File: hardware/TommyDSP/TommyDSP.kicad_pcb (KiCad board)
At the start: 2 copper layers, 85 x 85 mm, 143 parts, among them J401 Conn_01x02_Pin, J501 USB_C_Receptacle_USB2.0_16P, J502 AudioJack3_SwitchTR, J503 XH-2.50mm Horizontal, J504 AudioJack3_SwitchTR, J505 EXT.IN, J506 AudioJack3_SwitchTR, J507 XH-2.50mm Horizontal, J508 EXT.OUT, J509 Conn_01x03_Pin, J510 AudioJack3_SwitchTR, J511 Micro_SD_Card_Det1, J512 Qwiic, Q401 AO3401A, SW201 SW_Push, SW202 SW_Push, SW501 RotaryEncoder_Switch_MP, U201 W25Q128JVS, U202 DNF, U203 RP2350_60QFN, U301 ES8388, U401 TPS7A2033PDBVR, U402 TPS62A01APDDC, U403 TP4056-42-ESOP8, Y201 ABM8-272-T3

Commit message: hardware: minor tweaks
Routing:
- net GND: vias 815 -> 820

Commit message: hardware: minor tweaks
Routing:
- net GND: vias 820 -> 824
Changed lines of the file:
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@@
 	)
 	(via
+		(at 147.575 82.1)
+		(size 0.6)
+		(drill 0.3)
+		(layers "F.Cu" "B.Cu")
+		(free yes)
+		(net 2)
+	)
+	(via
 		(at 123 136.55)
 		(size 0.6)
@@
 	)
 	(via
+		(at 142.65 81.55)
+		(size 0.6)
+		(drill 0.3)
+		(layers "F.Cu" "B.Cu")
+		(free yes)
+		(net 2)
+	)
+	(via
 		(at 162.695 141.01)
 		(size 0.6)
@@
 	)
 	(via
+		(at 122.7 87.05)
+		(size 0.6)
+		(drill 0.3)
+		(layers "F.Cu" "B.Cu")
+		(free yes)
+		(net 2)
+	)
+	(via
 		(at 195.715 143.55)
 		(size 0.6)
@@
 		(size 0.6)
 		(drill 0.3)
+		(layers "F.Cu" "B.Cu")
+		(free yes)
+		(net 2)
+	)
+	(via
+		(at 138.25 81.575)
+		(size 0.6)
+		(drill 0.3)

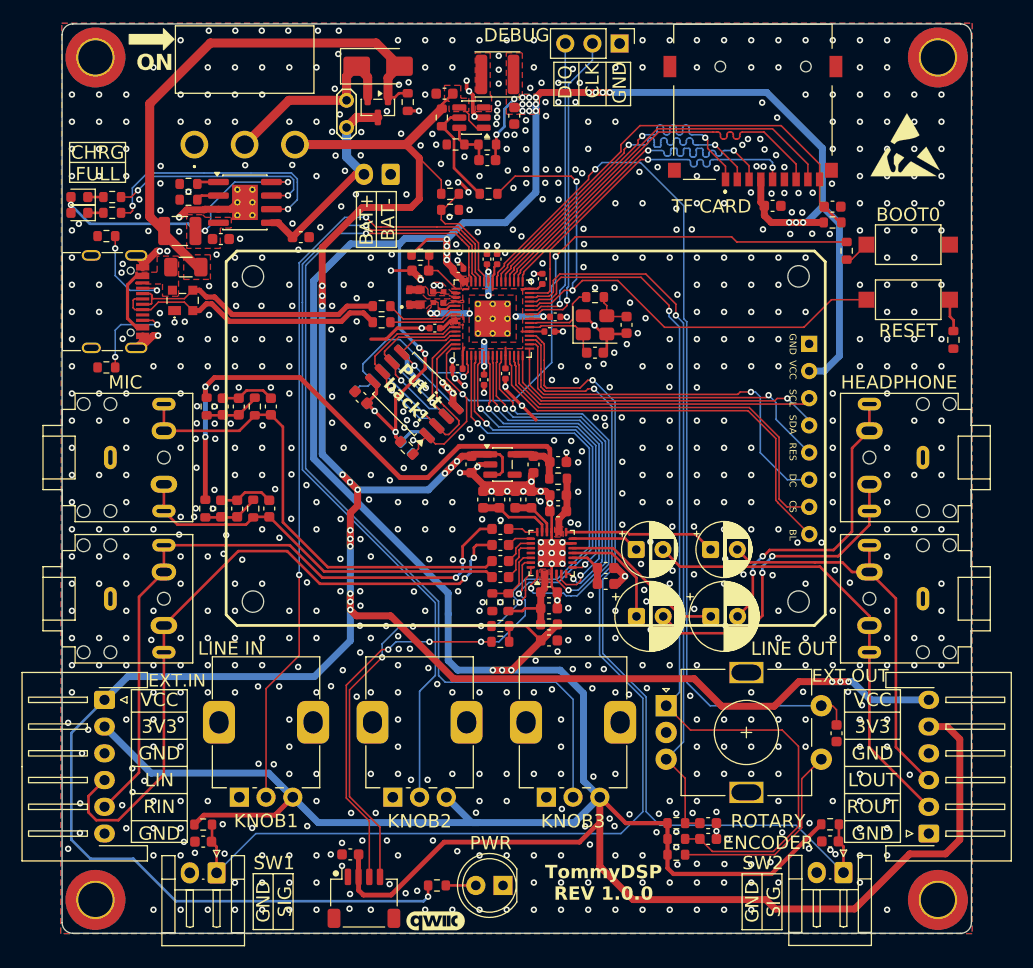
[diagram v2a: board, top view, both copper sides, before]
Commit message: hardware: adjust value of BUCK feedback resistors
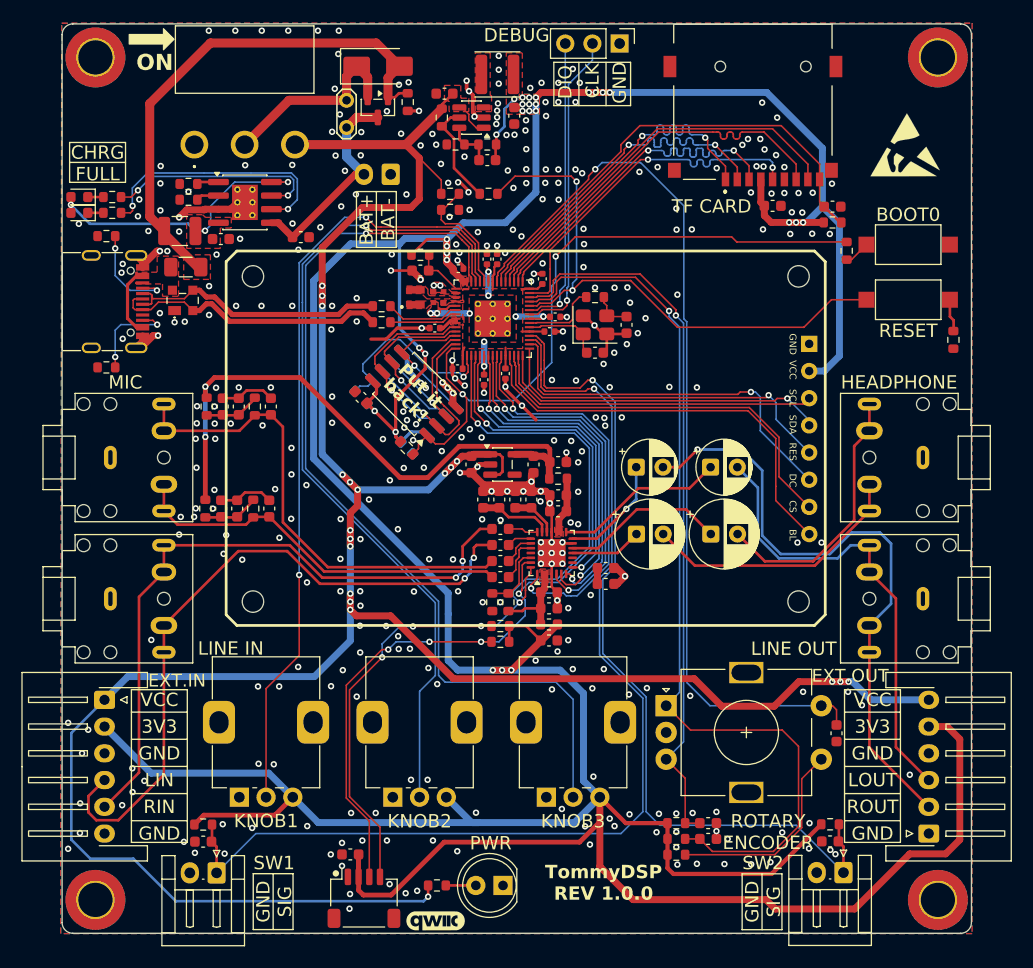
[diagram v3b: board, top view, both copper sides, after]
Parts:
- C316, C317: value 220u -> 220u 6.3v
- R403: value 500k -> 499k
- R405: value 225k -> 115k
- R406: value 50k -> 25.5k
- moved REF** 49.4 mm to (228.1, 107.0)
- moved C316 7.70 mm to (181.8, 116.0)
- moved C317 7.70 mm to (174.8, 116.0)
- moved C318 7.70 mm to (181.8, 109.8)
- moved C319 7.70 mm to (174.8, 109.8)
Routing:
- net /LINEOUT_R: track 42.0 -> 58.6 mm, vias 0 -> 1
- net /LINEOUT_L: track 37.5 -> 43.3 mm
- net /HPOUT_R: track 30.6 -> 25.1 mm, vias 2 -> 0
- net /Audio/ROUT2: track 6.38 -> 10.5 mm, vias 0 -> 1
- net /Audio/ROUT1: track 10.5 -> 6.71 mm
- net /HPOUT_L: track 28.5 -> 25.0 mm, vias 2 -> 0
- net /Audio/VREF: track 4.24 -> 1.52 mm
- net /Audio/LOUT2: track 14.2 -> 16.0 mm
- net /LCD_SPI_CS: track 38.3 -> 37.1 mm
- net /LCD_DC: track 36.9 -> 35.7 mm
- net GND: vias 824 -> 368

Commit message: hardware: add compatibility for WM8988 CODEC
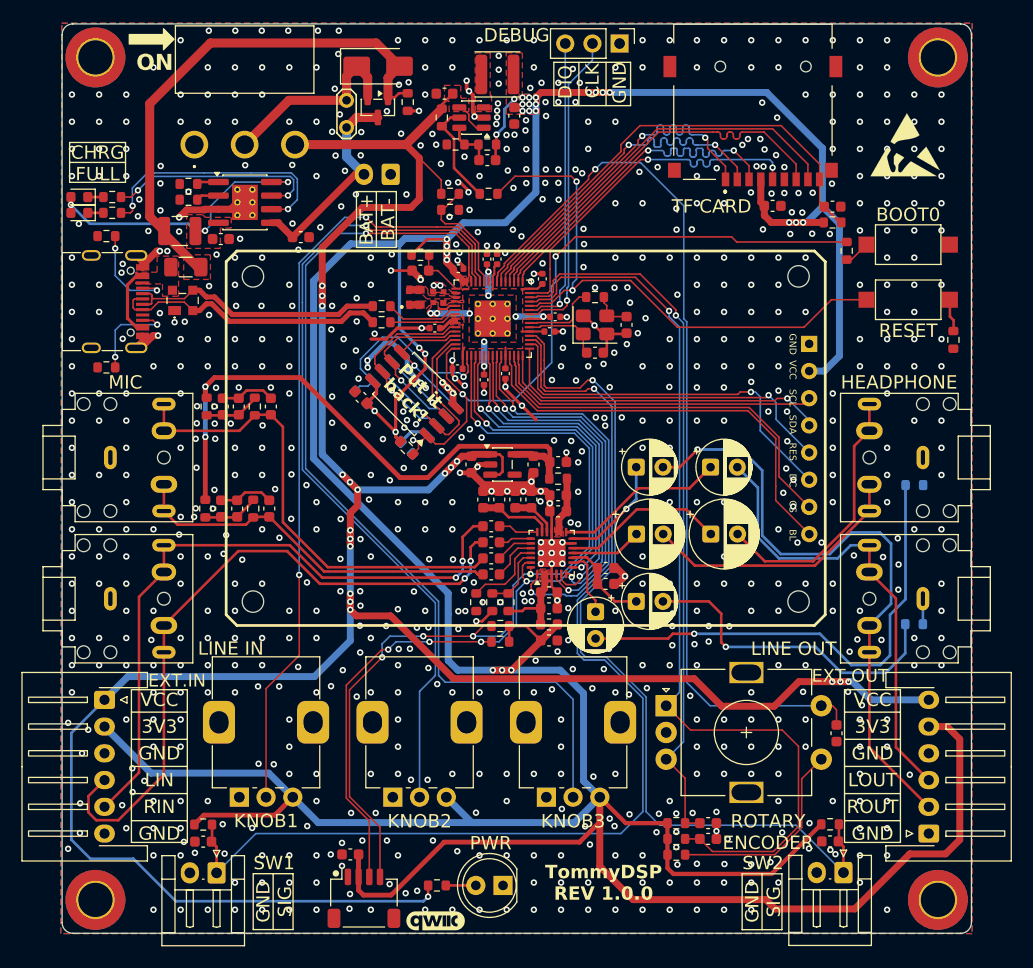
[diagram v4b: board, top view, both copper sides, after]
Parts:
- added C326: 4.7u, Capacitor_THT:CP_Radial_D5.0mm_P2.50mm, F.Cu at (174.8, 122.3)
- added C327: 4.7u, Capacitor_THT:CP_Radial_D5.0mm_P2.50mm, F.Cu at (171.0, 123.3)
- added R308: 0, Resistor_SMD:R_0603_1608Metric, B.Cu at (200.8, 124.5)
- added R309: 0, Resistor_SMD:R_0603_1608Metric, B.Cu at (200.8, 111.5)
- added R310: 0, Resistor_SMD:R_0603_1608Metric, F.Cu at (159.8, 122.4)
- U301: value ES8388 -> ES8388/WM8988
- moved REF** 48.7 mm to (179.6, 102.2)
- moved C312 0.89 mm to (161.2, 119.8)
- moved C313 0.89 mm to (161.2, 118.3)
- moved C314 0.89 mm to (161.2, 116.8)
- moved C315 0.89 mm to (161.2, 115.3)
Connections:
- net /Audio/VREF renamed /Audio/VREF/LCOM
- U301 pad 25: unconnected-(U301-NC-Pad25) -> Net-(U301-NC/MODE)
- U301 pad 9: unconnected-(U301-NC-Pad9) -> Net-(U301-NC/HPCOM)
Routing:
- net Net-(C327-Pad2): track 0.00 -> 45.8 mm, vias 0 -> 1
- net Net-(C326-Pad2): track 0.00 -> 30.5 mm, vias 0 -> 1
- net GND: track 102.2 -> 111.3 mm, vias 368 -> 820
- net Net-(U301-NC/MODE): track 0.00 -> 7.51 mm
- net /Audio/VREF/LCOM: track 1.52 -> 9.00 mm
- net Net-(U301-NC/HPCOM): track 0.00 -> 6.26 mm
- net /PEDAL_2: track 79.5 -> 82.3 mm
- net /PEDAL_1: track 99.7 -> 102.6 mm
- net /CODEC_I2C_SDA: track 81.1 -> 79.6 mm
- net /CODEC_I2C_SCL: track 80.7 -> 79.4 mm
- net /MIC_L: track 36.3 -> 35.4 mm
- net Net-(U301-RIN2): track 2.80 -> 3.75 mm
- net /MCU-Core/GPIO0: track 18.1 -> 18.9 mm
- net Net-(U301-LIN2): track 2.32 -> 3.07 mm
- net /MIC_R: track 45.2 -> 44.4 mm
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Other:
- board text added: "CODEC POSITION: X:166.9 mm Y:117.825 mm"
